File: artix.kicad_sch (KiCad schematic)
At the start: 50 parts, among them U2 XC7A200T-FBG484

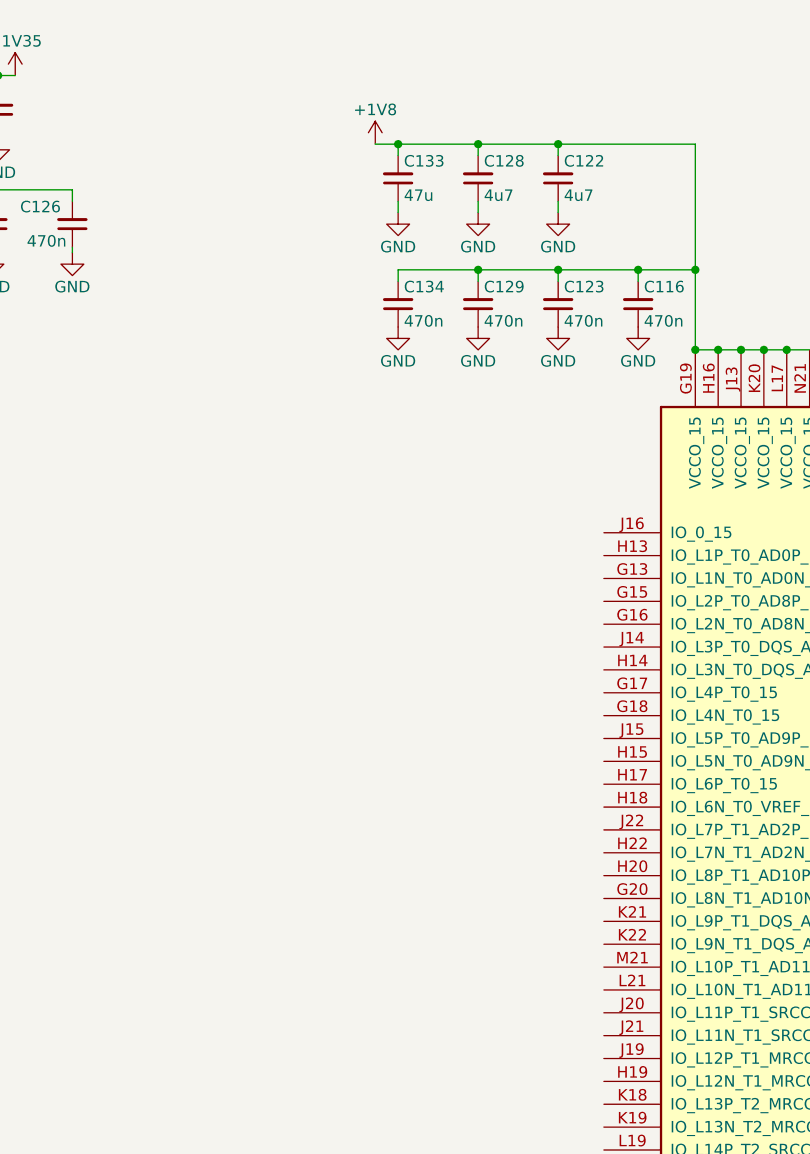
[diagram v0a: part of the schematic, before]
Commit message: added adc
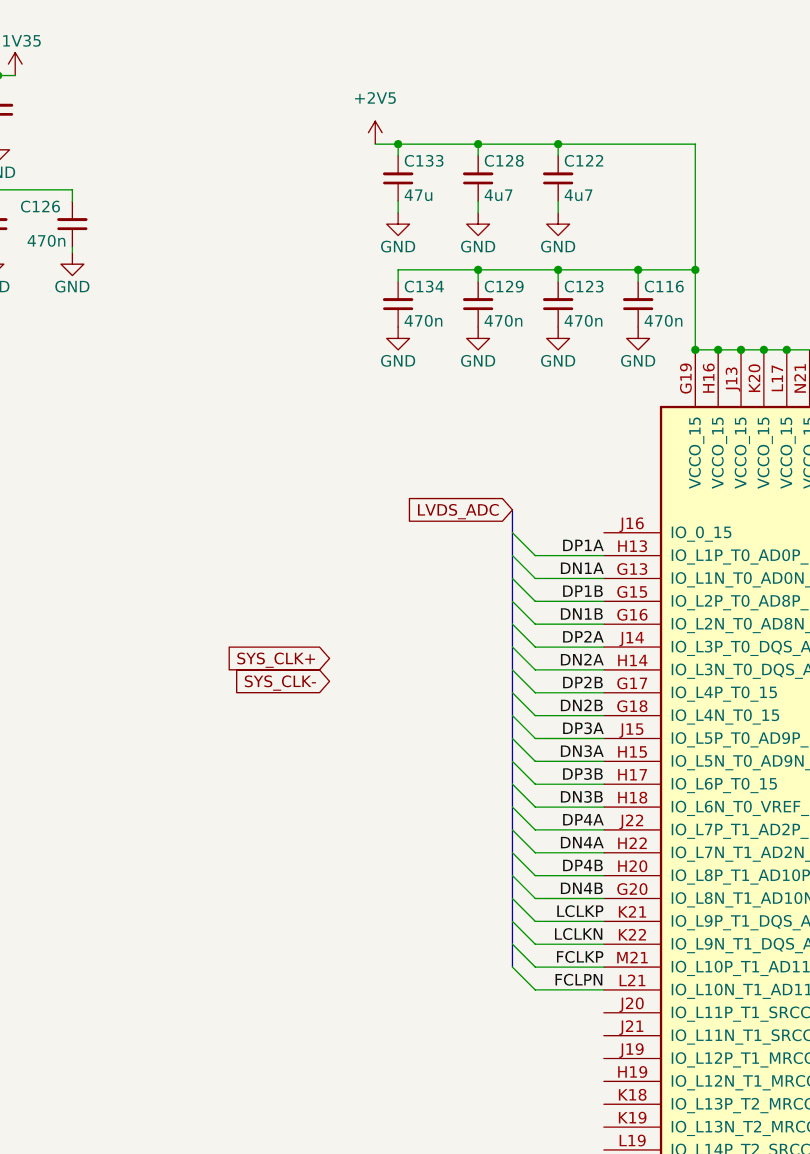
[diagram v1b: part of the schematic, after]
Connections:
- net +1V8: no longer C116.2, C122.2, C123.2, C128.2, C129.2, C133.2, C134.2, U2.G19 (VCCO_15), U2.H16 (VCCO_15), U2.J13 (VCCO_15), U2.K20 (VCCO_15), U2.L17 (VCCO_15), U2.N21 (VCCO_15)
- net DN1A: now reaches U2.G13 (IO_L1N_T0_AD0N_15)
- net DP1B: now reaches U2.G15 (IO_L2P_T0_AD8P_15)
- net DN1B: now reaches U2.G16 (IO_L2N_T0_AD8N_15)
- net DP2B: now reaches U2.G17 (IO_L4P_T0_15)
- net DN2B: now reaches U2.G18 (IO_L4N_T0_15)
- net DN4B: now reaches U2.G20 (IO_L8N_T1_AD10N_15)
- net DP1A: now reaches U2.H13 (IO_L1P_T0_AD0P_15)
- net DN2A: now reaches U2.H14 (IO_L3N_T0_DQS_AD1N_15)
- net DN3A: now reaches U2.H15 (IO_L5N_T0_AD9N_15)
- net DP3B: now reaches U2.H17 (IO_L6P_T0_15)
- net DN3B: now reaches U2.H18 (IO_L6N_T0_VREF_15)
- net DP4B: now reaches U2.H20 (IO_L8P_T1_AD10P_15)
- net DN4A: now reaches U2.H22 (IO_L7N_T1_AD2N_15)
- net DP2A: now reaches U2.J14 (IO_L3P_T0_DQS_AD1P_15)
- net DP3A: now reaches U2.J15 (IO_L5P_T0_AD9P_15)
- net DP4A: now reaches U2.J22 (IO_L7P_T1_AD2P_15)
- net LCLKP: now reaches U2.K21 (IO_L9P_T1_DQS_AD3P_15)
- net LCLKN: now reaches U2.K22 (IO_L9N_T1_DQS_AD3N_15)
- net FCLPN: now reaches U2.L21 (IO_L10N_T1_AD11N_15)
- net FCLKP: now reaches U2.M21 (IO_L10P_T1_AD11P_15)
- new net +2V5: C116.2, C122.2, C123.2, C128.2, C129.2, C133.2, C134.2, U2.G19 (VCCO_15), U2.H16 (VCCO_15), U2.J13 (VCCO_15), U2.K20 (VCCO_15), U2.L17 (VCCO_15), U2.N21 (VCCO_15)

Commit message: added clk
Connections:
- net FCLKP: now also U2.K18 (IO_L13P_T2_MRCC_15); no longer U2.M21 (IO_L10P_T1_AD11P_15)
- net FCLPN: now also U2.K19 (IO_L13N_T2_MRCC_15); no longer U2.L21 (IO_L10N_T1_AD11N_15)
- net LCLKN: now also U2.H19 (IO_L12N_T1_MRCC_15); no longer U2.K22 (IO_L9N_T1_DQS_AD3N_15)
- net LCLKP: now also U2.J19 (IO_L12P_T1_MRCC_15); no longer U2.K21 (IO_L9P_T1_DQS_AD3P_15)
- net ADC_SDATA: now reaches U2.F13 (IO_L1P_T0_16)
- net ADC_CSN: now reaches U2.F14 (IO_L1N_T0_16)
- net ADC_SCLK: now reaches U2.F15 (IO_0_16)
- no-connect marks 180 -> 177
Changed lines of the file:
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@@
 	)
 	(no_connect
-		(at 541.02 92.71)
-	)
-	(no_connect
 		(at 541.02 143.51)
 	)
 	(no_connect
-		(at 541.02 97.79)
-	)
-	(no_connect
 		(at 541.02 207.01)
 	)
@@
 	)
 	(no_connect
-		(at 541.02 95.25)
-	)
-	(no_connect
 		(at 140.97 176.53)
 	)
@@
 	)
 	(bus_entry
-		(at 431.8 95.25)
+		(at 431.8 158.75)
 		(size -2.54 -2.54)
 		(stroke
@@
 	)
 	(bus_entry
-		(at 431.8 135.89)
+		(at 431.8 95.25)
 		(size -2.54 -2.54)
 		(stroke
@@
 	)
 	(bus_entry
-		(at 431.8 110.49)
+		(at 431.8 153.67)
 		(size -2.54 -2.54)
 		(stroke
@@
 	)
 	(bus_entry
-		(at 431.8 128.27)
+		(at 431.8 110.49)
 		(size -2.54 -2.54)
 		(stroke
@@
 	)
 	(bus_entry
-		(at 431.8 140.97)
+		(at 431.8 128.27)
 		(size -2.54 -2.54)
 		(stroke
@@
 	)
 	(bus_entry
-		(at 431.8 143.51)
+		(at 431.8 151.13)
 		(size -2.54 -2.54)
 		(stroke
@@
 	)
 	(bus_entry
-		(at 431.8 138.43)
+		(at 431.8 105.41)
 		(size -2.54 -2.54)
 		(stroke
@@
 	)
 	(bus_entry
-		(at 431.8 105.41)
+		(at 431.8 156.21)
 		(size -2.54 -2.54)
 		(stroke
@@
 	(wire
 		(pts
-			(xy 439.42 138.43) (xy 431.8 138.43)
+			(xy 238.76 49.53) (xy 238.76 50.8)
 		)
 		(stroke
@@
 	(wire
 		(pts
-			(xy 238.76 49.53) (xy 238.76 50.8)
+			(xy 22.86 41.91) (xy 22.86 43.18)
 		)
 		(stroke
@@
 	(wire
 		(pts
-			(xy 22.86 41.91) (xy 22.86 43.18)
+			(xy 439.42 158.75) (xy 431.8 158.75)
 		)
 		(stroke
@@
 	(wire
 		(pts
+			(xy 541.02 97.79) (xy 547.37 97.79)
+		)
+		(stroke
+			(width 0)
+			(type default)
+		)
+	)
+	(wire
+		(pts
 			(xy 380.365 60.96) (xy 380.365 61.595)
 		)
@@
 	(wire
 		(pts
-			(xy 439.42 135.89) (xy 431.8 135.89)
+			(xy 273.05 293.37) (xy 284.48 293.37)
 		)
 		(stroke
@@
 	(wire
 		(pts
-			(xy 273.05 293.37) (xy 284.48 293.37)
+			(xy 541.02 95.25) (xy 547.37 95.25)
 		)
 		(stroke
@@
 	(bus
 		(pts
-			(xy 429.26 90.17) (xy 429.26 140.97)
+			(xy 429.26 90.17) (xy 429.26 156.21)
 		)
 		(stroke
@@
 	(wire
 		(pts
-			(xy 439.42 143.51) (xy 431.8 143.51)
+			(xy 541.02 92.71) (xy 547.37 92.71)
 		)
 		(stroke
@@
 	(wire
 		(pts
+			(xy 439.42 153.67) (xy 431.8 153.67)
+		)
+		(stroke
+			(width 0)
+			(type default)
+		)
+	)
+	(wire
+		(pts
 			(xy 439.42 105.41) (xy 431.8 105.41)
 		)
@@
 	(wire
 		(pts
+			(xy 439.42 156.21) (xy 431.8 156.21)
+		)
+		(stroke
+			(width 0)
+			(type default)
+		)
+	)
+	(wire
+		(pts
 			(xy 425.45 55.88) (xy 425.45 57.15)
 		)
@@
 	(wire
 		(pts
-			(xy 439.42 140.97) (xy 431.8 140.97)
-		)
-		(stroke
-			(width 0)
-			(type default)
-		)
-	)
-	(wire
-		(pts
 			(xy 146.05 48.26) (xy 146.05 48.895)
 		)
@@
 	(wire
 		(pts
+			(xy 439.42 151.13) (xy 431.8 151.13)
+		)
+		(stroke
+			(width 0)
+			(type default)
+		)
+	)
+	(wire
+		(pts
 			(xy 546.1 50.8) (xy 546.1 52.07)
 		)
@@
 		)
 	)
-	(label "DP4B"
-		(at 439.42 130.81 180)
+	(label "LCLKN"
+		(at 439.42 153.67 180)
 		(effects
 			(font
@@
 		)
 	)
-	(label "DP3B"
-		(at 439.42 120.65 180)
+	(label "FCLKP"
+		(at 439.42 156.21 180)
 		(effects
 			(font
@@
 		)
 	)
-	(label "FCLPN"
-		(at 439.42 143.51 180)
+	(label "DP4B"
+		(at 439.42 130.81 180)
+		(effects
+			(font
+				(size 1.27 1.27)
+			)
+			(justify right bottom)
+		)
+	)
+	(label "DP3B"
+		(at 439.42 120.65 180)
 		(effects
 			(font
@@
 		)
 	)
-	(label "FCLKP"
-		(at 439.42 140.97 180)
-		(effects
-			(font
-				(size 1.27 1.27)
-			)
-			(justify right bottom)
-		)
-	)
 	(label "DN3A"
 		(at 439.42 118.11 180)
@@
 		)
 	)
-	(label "DP3A"
-		(at 439.42 115.57 180)
+	(label "FCLPN"
+		(at 439.42 158.75 180)
 		(effects
 			(font
@@
 		)
 	)
-	(label "LCLKP"
-		(at 439.42 135.89 180)
+	(label "DP3A"
+		(at 439.42 115.57 180)
 		(effects
 			(font
@@
 		)
 	)
-	(label "LCLKN"
-		(at 439.42 138.43 180)
+	(label "DN2B"
+		(at 439.42 113.03 180)
 		(effects
 			(font
@@
 		)
 	)
-	(label "DN2B"
-		(at 439.42 113.03 180)
+	(label "LCLKP"
+		(at 439.42 151.13 180)
 		(effects
 			(font
@@
 		)
 	)
+	(global_label "ADC_SCLK"
+		(shape passive)
+		(at 547.37 92.71 0)
+		(effects
+			(font
+				(size 1.27 1.27)
+			)
+			(justify left)
+		)
+		(property "Intersheetrefs" "${INTERSHEET_REFS}"
+			(at 547.37 92.71 0)
+			(hide yes)
+			(show_name no)
+			(do_not_autoplace no)
+			(effects
+				(font
+					(size 1.27 1.27)
+				)
+			)
+		)
+	)
 	(global_label "QSPI_CS"
 		(shape input)
@@
 		)
 	)
+	(global_label "ADC_CSN"
+		(shape passive)
+		(at 547.37 97.79 0)
+		(effects
+			(font
+				(size 1.27 1.27)
+			)
+			(justify left)
+		)
+		(property "Intersheetrefs" "${INTERSHEET_REFS}"
+			(at 547.37 97.79 0)
+			(hide yes)
+			(show_name no)
+			(do_not_autoplace no)
+			(effects
+				(font
+					(size 1.27 1.27)
+				)
+			)
+		)
+	)
 	(global_label "MGTPRX2_216+"
 		(shape bidirectional)
@@
 		)
 	)
-	(global_label "SYS_CLK-"
-		(shape input)
-		(at 408.94 109.22 180)
-		(fields_autoplaced yes)
+	(global_label "ADC_SDATA"
+		(shape passive)
+		(at 547.37 95.25 0)
 		(effects
 			(font
 				(size 1.27 1.27)
 			)
-			(justify right)
+			(justify left)
 		)
 		(property "Intersheetrefs" "${INTERSHEET_REFS}"
-			(at 396.3391 109.22 0)
+			(at 547.37 95.25 0)
 			(hide yes)
 			(show_name no)
@@
 					(size 1.27 1.27)
 				)
-				(justify right)
 			)
 		)
@@
 			)
 		)
-	)
-	(global_label "SYS_CLK+"
-		(shape input)
-		(at 408.94 106.68 180)
-		(fields_autoplaced yes)
-		(effects
-			(font
-				(size 1.27 1.27)
-			)
-			(justify right)
-		)
-		(property "Intersheetrefs" "${INTERSHEET_REFS}"
-			(at 396.3391 106.68 0)
-			(hide yes)
-			(show_name no)
-			(do_not_autoplace no)
-			(effects
-				(font
-					(size 1.27 1.27)
-				)
-				(justify right)
-			)
-		)
